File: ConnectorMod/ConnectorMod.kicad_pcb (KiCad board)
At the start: 2 copper layers, 99 x 90 mm, 74 parts, among them J1 PJ-325, J2 PJ-325, J3 PJ-325, J4 PJ-066A, J5 BAT1, J6 BAT2, Q1 MMBT3906, Q2 MMBT3906, Q3 MMBT3906, Q4 MMBT3904, Q5 MMBT3904, U1 TLV2372, U2 TLP2366

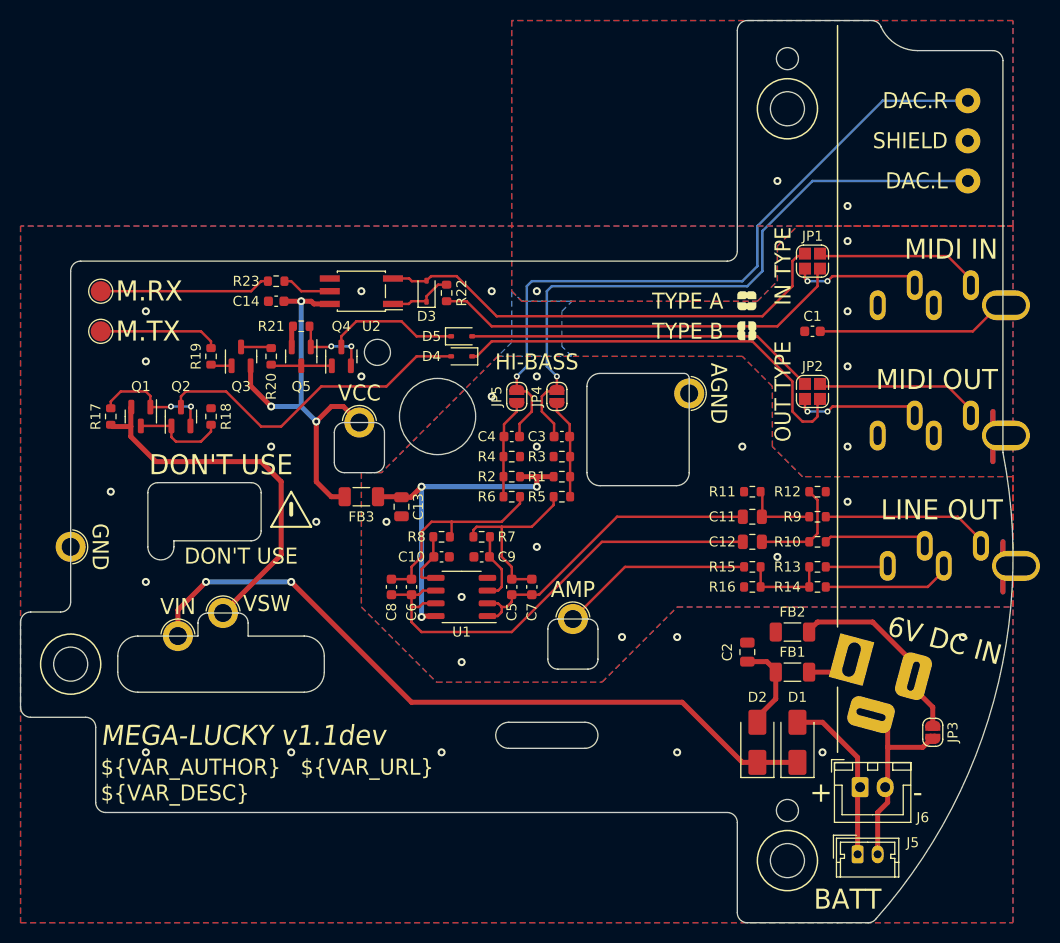
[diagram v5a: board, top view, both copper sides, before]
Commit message: Make all audio caps at least 0805
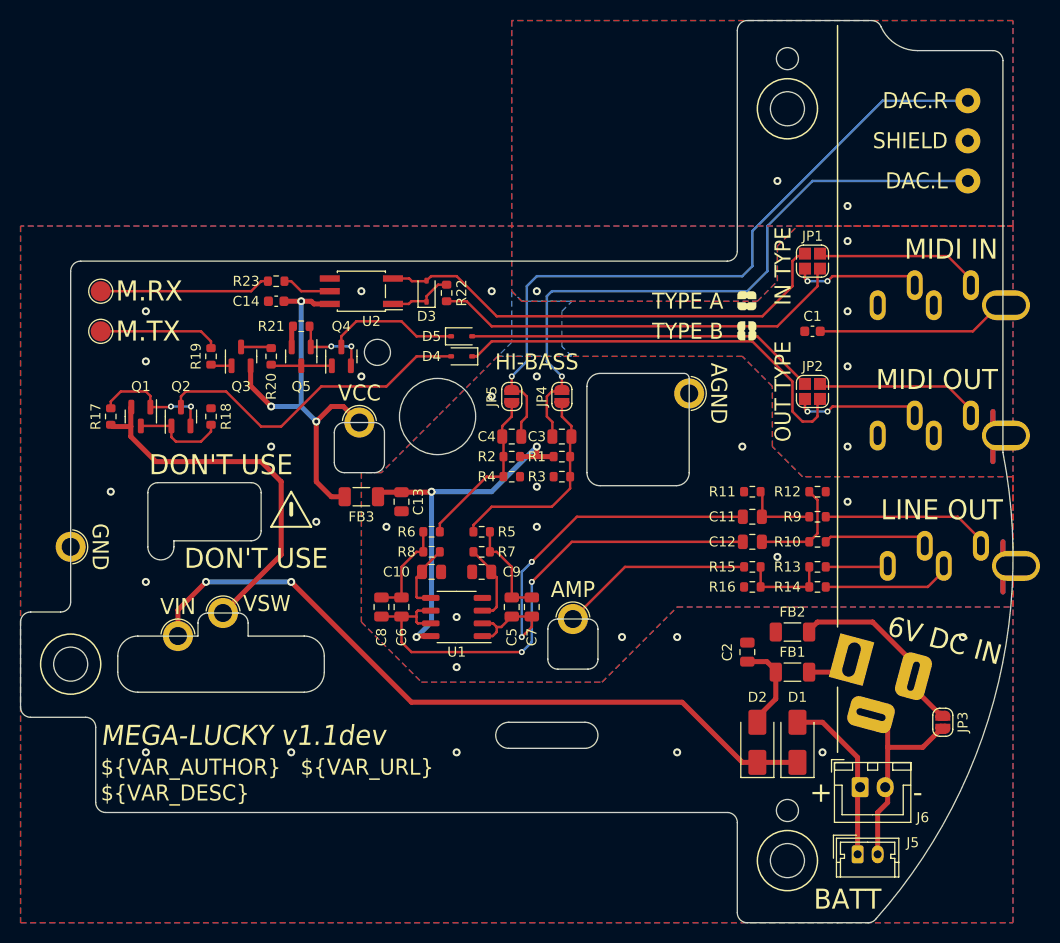
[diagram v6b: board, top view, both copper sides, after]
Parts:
- C10, C3, C4, C5, C6, C7, C8, C9: footprint Capacitor_SMD:C_0603_1608Metric -> Capacitor_SMD:C_0805_2012Metric
- moved R5 8.73 mm to (64.5, 76.0), turned to 0 degrees
- moved R6 8.73 mm to (59.5, 76.0), turned to 180 degrees
- moved C6 2.24 mm to (56.5, 83.5)
- moved C8 2.24 mm to (54.5, 83.5)
- moved U1 2.06 mm to (62.0, 84.5)
- moved C5 2.00 mm to (67.5, 83.5)
- moved C7 2.00 mm to (69.5, 83.5)
- moved R1 2.00 mm to (72.5, 68.5)
- moved R2 2.00 mm to (67.5, 68.5)
- moved R3 2.00 mm to (72.5, 70.5)
- moved R4 2.00 mm to (67.5, 70.5)
- moved C10 1.80 mm to (59.5, 80.0)
- moved R8 1.80 mm to (59.5, 78.0), turned to 0 degrees
- moved C9 1.50 mm to (64.5, 80.0)
- moved R7 1.50 mm to (64.5, 78.0), turned to 180 degrees
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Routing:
- net Net-(JP4-B): track 9.90 -> 20.8 mm
- net Net-(C6-Pad2): track 20.4 -> 9.85 mm
- net Net-(U1A--): track 31.4 -> 40.9 mm, vias 0 -> 2
- net Net-(C5-Pad2): track 18.2 -> 9.85 mm
- net Net-(JP5-B): track 9.90 -> 16.9 mm
- net Net-(U1B--): track 47.1 -> 52.6 mm, vias 0 -> 2
- net +3.3VA: track 35.1 -> 38.8 mm
- net -BATT: track 20.3 -> 21.7 mm
- net Net-(U1A-+): track 7.10 -> 8.04 mm
- net Net-(U1B-+): track 5.99 -> 6.93 mm
